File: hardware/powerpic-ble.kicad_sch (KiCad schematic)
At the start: 10 parts

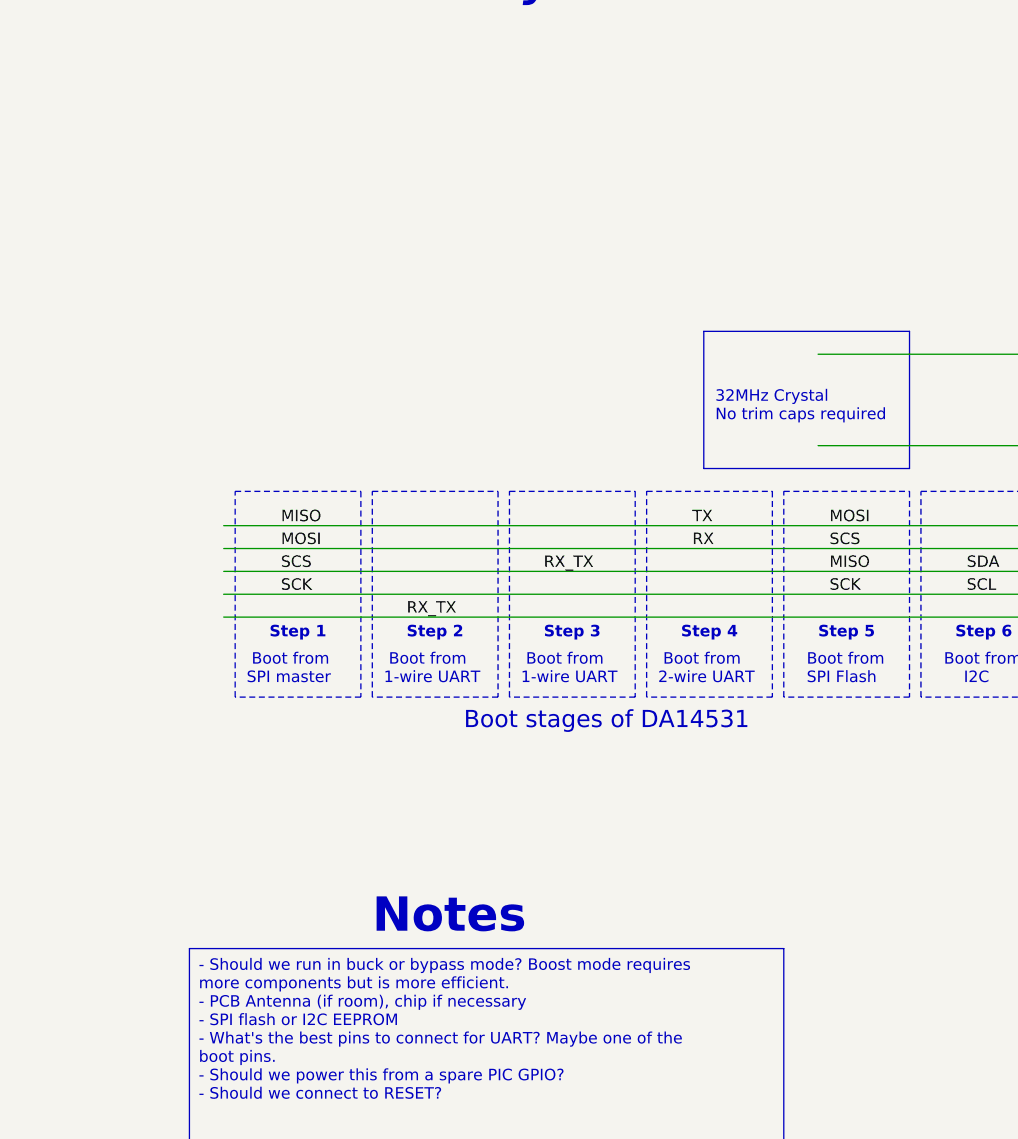
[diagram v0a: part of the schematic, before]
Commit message: hardware: Minor changes. Mostly playing around in the new kicad nightly.
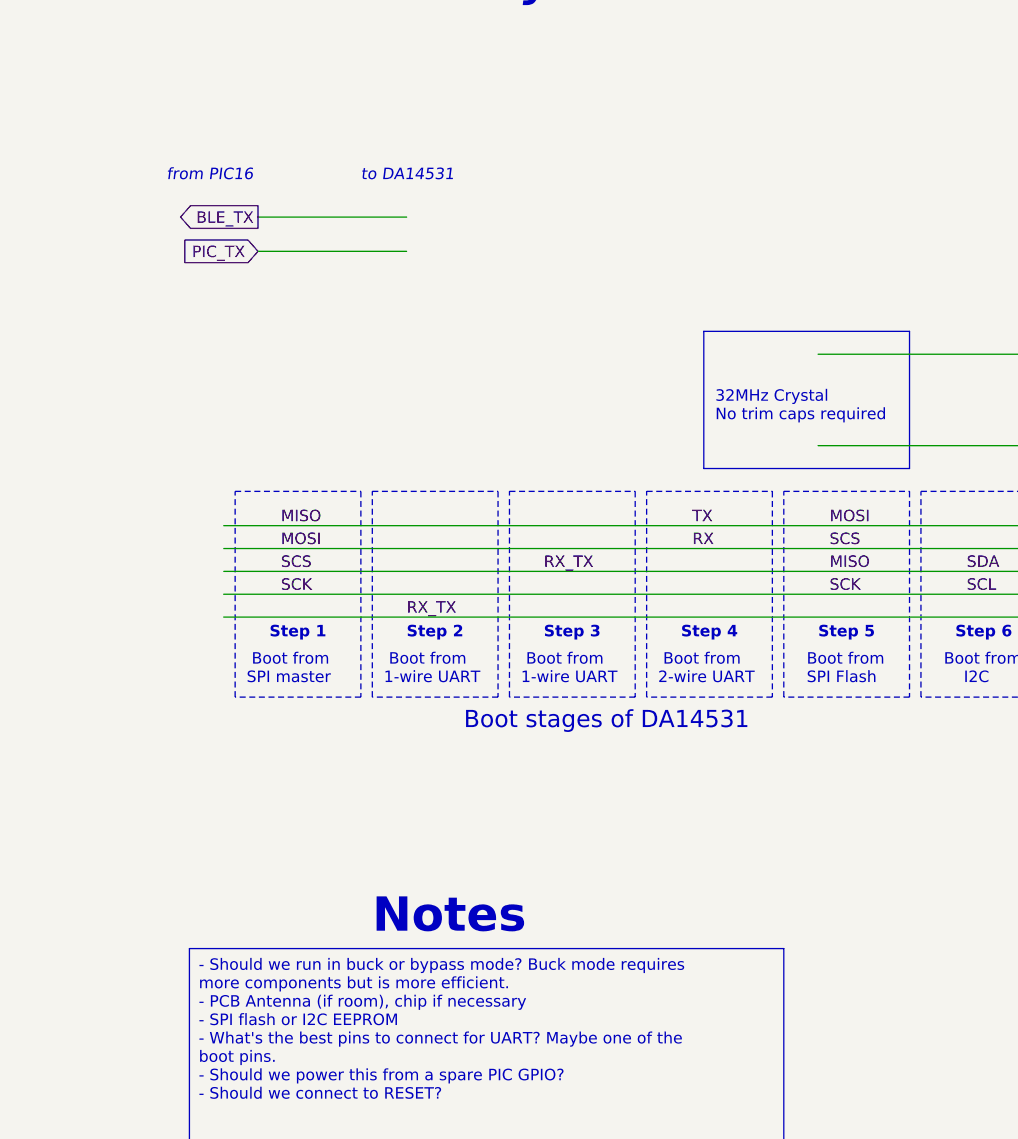
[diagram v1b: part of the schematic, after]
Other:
- note added: "from PIC16"
- note added: "to DA14531"
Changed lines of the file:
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@@
+    (stroke (width 0) (type default))
+  )
+  (wire (pts (xy 39.37 69.85) (xy 55.88 69.85))
+    (stroke (width 0) (type default))
+  )
+  (wire (pts (xy 39.37 73.66) (xy 55.88 73.66))
     (stroke (width 0) (type default))
   )
@@
     (fill (type none))
   )
-  (text_box "- Should we run in buck or bypass mode? Boost mode requires more components but is more efficient.\n- PCB Antenna (if room), chip if necessary\n- SPI flash or I2C EEPROM\n- What's the best pins to connect for UART? Maybe one of the boot pins.\n- Should we power this from a spare PIC GPIO?\n- Should we connect to RESET?"
+  (text_box "- Should we run in buck or bypass mode? Buck mode requires more components but is more efficient.\n- PCB Antenna (if room), chip if necessary\n- SPI flash or I2C EEPROM\n- What's the best pins to connect for UART? Maybe one of the boot pins.\n- Should we power this from a spare PIC GPIO?\n- Should we connect to RESET?"
     (at 31.75 151.13 0) (size 66.04 45.72)
     (stroke (width 0) (type default))
@@
     (effects (font (size 1.27 1.27) italic) (justify left bottom))
   )
+  (text "to DA14531" (at 50.8 66.04 0)
+    (effects (font (size 1.27 1.27) italic) (justify left bottom))
+  )
   (text "Step 1" (at 40.64 116.84 0)
     (effects (font (size 1.27 1.27) bold) (justify left bottom))
+  )
+  (text "from PIC16" (at 29.21 66.04 0)
+    (effects (font (size 1.27 1.27) italic) (justify left bottom))
   )
   (text "Step 6" (at 116.84 116.84 0)
@@
     (effects (font (size 1.27 1.27)) (justify left bottom))
   )
+  (global_label "BLE_TX" (shape output) (at 39.37 69.85 180) (fields_autoplaced)
+    (effects (font (size 1.27 1.27)) (justify right))
+    (property "Intersheetrefs" "${INTERSHEET_REFS}" (id 0) (at 30.0312 69.85 0)
+      (effects (font (size 1.27 1.27)) (justify right) hide)
+    )
+  )
+  (global_label "PIC_TX" (shape input) (at 39.37 73.66 180) (fields_autoplaced)
+    (effects (font (size 1.27 1.27)) (justify right))
+    (property "Intersheetrefs" "${INTERSHEET_REFS}" (id 0) (at 30.3335 73.66 0)
+      (effects (font (size 1.27 1.27)) (justify right) hide)
+    )
+  )
   (symbol (lib_id "Device:C") (at 142.24 59.69 0) (unit 1)
